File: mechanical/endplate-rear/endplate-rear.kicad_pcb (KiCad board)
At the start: 2 copper layers, 88 x 38 mm, 0 parts

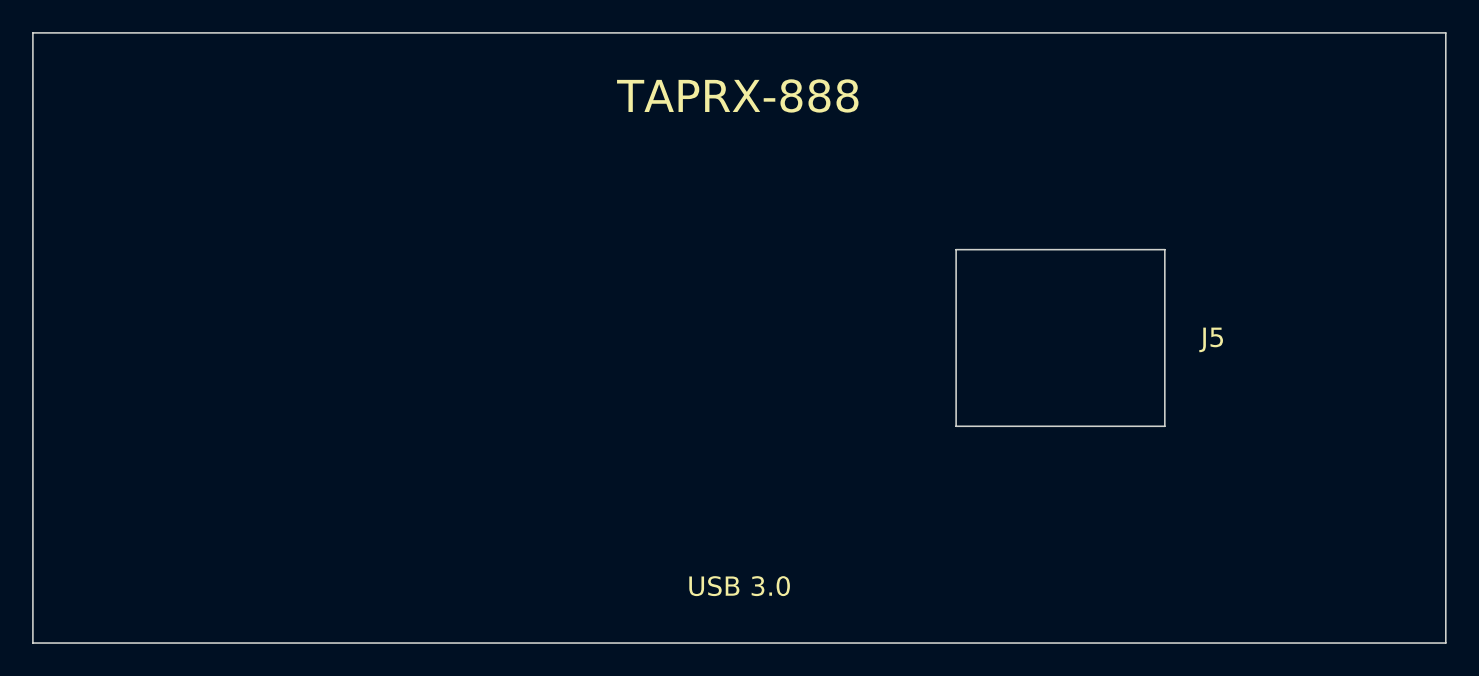
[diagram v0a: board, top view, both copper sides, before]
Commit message: mechanical: rebuild end plates from enclosure DXF geometry
Replace the nominal 88x38 starter outline with real geometry sectioned from the
enclosure extrusion end (FreeCAD DXF, centred on 0,0):

- outline 88x38 mm, corner radius 4.5 (rounded rect: 4 edges + 4 arcs)
- four M3 corner mounting holes, Ø3.4 at (±41, ±14.21) -> the plate screws on;
  it is not a slide-in panel (the 84.2 mm groove is the internal PCB slot)

Connector cutout X's are the main board's real connector positions mapped to
plate-centred coords (plate-X = 44 + (board-X - 138)), verified against the PCB:

- front SMA J1/J3/J2/J4 at -27/-9/+9/+26.8 mm from centre
- rear USB J5 at +19 mm from centre; J11 (JTAG) internal, no cutout

Connector Y remains a placeholder at plate centre pending the PCB rail height +
connector centre heights (3D models); cutout sizes (SMA Ø6.5, USB 13x11) and the
rear X-mirror stay flagged on Cmts.User. Open in KiCad 10 to confirm it parses.

Co-Authored-By: Claude Opus 4.8 <noreply@anthropic.com>
Claude-Session: https://claude.ai/code/session_019A4jkTeNPLki8CdfTWEUwM
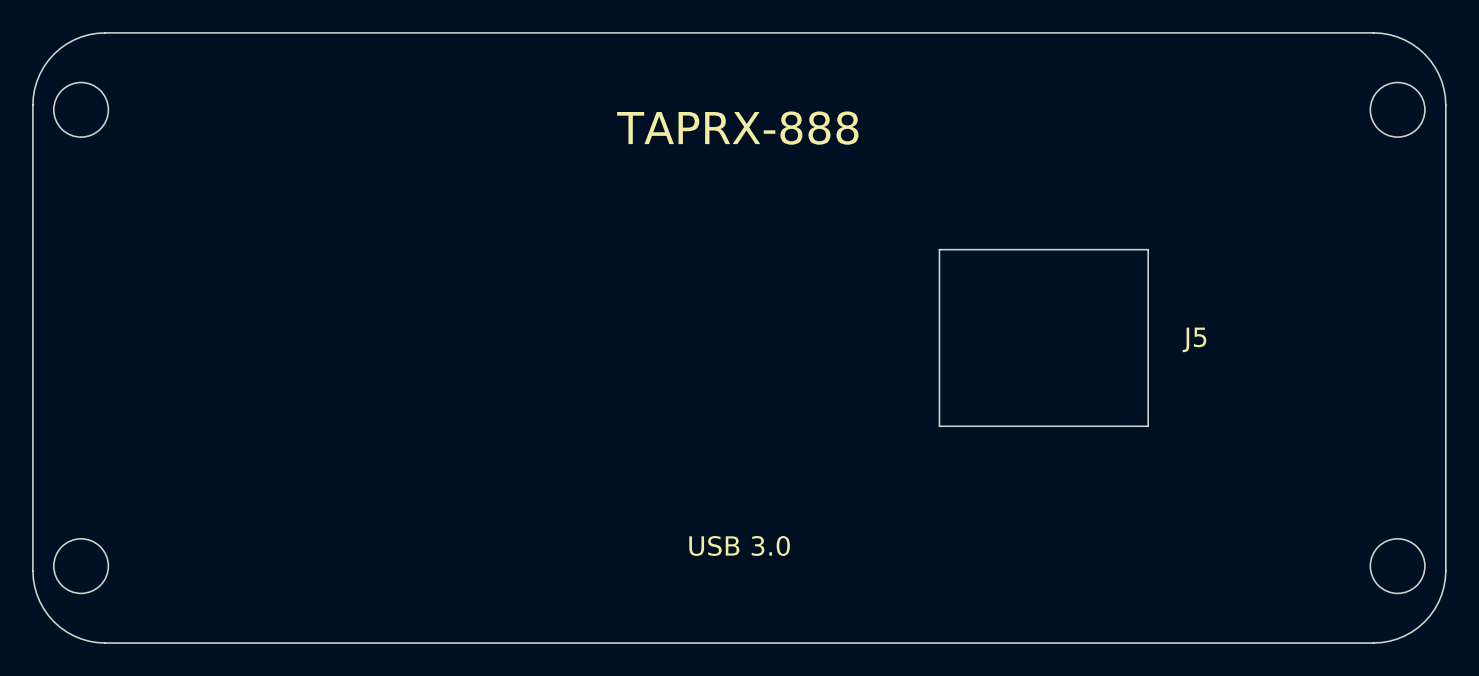
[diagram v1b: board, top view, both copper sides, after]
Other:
- outline, holes or cut-outs redrawn
- board text added: "REAR PLATE: confirm X-mirror vs assembly orientation. Outline+M3 corner holes from enclosure DXF (88x38 R4.5, holes Ø3.4 @ +/-41,+/-14.21). CONNECTOR Y IS PLACEHOLDER at plate centre -- set from PCB rail height + connector centre heights (3D models). SMA Ø6.5 / USB 13x11 verify vs parts. Open in KiCad 10 to confirm parse."
- board text removed: "REAR PLATE: confirm X-mirror vs assembly orientation. PLACEHOLDER GEOMETRY - verify vs enclosure STEP: plate 88x38 nominal (check groove fit); connector Y at plate centre (needs board height in rail + connector centre height); SMA D6.5 / USB 13x11 (verify vs parts)."
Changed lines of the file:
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@@
 		(company "TAPR")
 		(comment 1 "Non-functional enclosure end plate")
-		(comment 2 "Starter geometry -- verify against enclosure STEP")
+		(comment 2 "Outline+holes from enclosure DXF; connector Y placeholder")
 	)
 	(layers
@@
 	(net 0 "")
 	(gr_line
-		(start 0 0)
-		(end 88.0 0)
-		(stroke
-			(width 0.1)
-			(type default)
-		)
-		(layer "Edge.Cuts")
-	)
-	(gr_line
-		(start 88.0 0)
-		(end 88.0 38.0)
-		(stroke
-			(width 0.1)
-			(type default)
-		)
-		(layer "Edge.Cuts")
-	)
-	(gr_line
-		(start 88.0 38.0)
-		(end 0 38.0)
-		(stroke
-			(width 0.1)
-			(type default)
-		)
-		(layer "Edge.Cuts")
-	)
-	(gr_line
-		(start 0 38.0)
-		(end 0 0)
-		(stroke
-			(width 0.1)
-			(type default)
-		)
-		(layer "Edge.Cuts")
-	)
-	(gr_line
-		(start 57.5 13.5)
-		(end 70.5 13.5)
-		(stroke
-			(width 0.1)
-			(type default)
-		)
-		(layer "Edge.Cuts")
-	)
-	(gr_line
-		(start 70.5 13.5)
-		(end 70.5 24.5)
-		(stroke
-			(width 0.1)
-			(type default)
-		)
-		(layer "Edge.Cuts")
-	)
-	(gr_line
-		(start 70.5 24.5)
-		(end 57.5 24.5)
-		(stroke
-			(width 0.1)
-			(type default)
-		)
-		(layer "Edge.Cuts")
-	)
-	(gr_line
-		(start 57.5 24.5)
-		(end 57.5 13.5)
+		(start 4.5 0)
+		(end 83.5 0)
+		(stroke
+			(width 0.1)
+			(type default)
+		)
+		(layer "Edge.Cuts")
+	)
+	(gr_line
+		(start 88.0 4.5)
+		(end 88.0 33.5)
+		(stroke
+			(width 0.1)
+			(type default)
+		)
+		(layer "Edge.Cuts")
+	)
+	(gr_line
+		(start 83.5 38.0)
+		(end 4.5 38.0)
+		(stroke
+			(width 0.1)
+			(type default)
+		)
+		(layer "Edge.Cuts")
+	)
+	(gr_line
+		(start 0 33.5)
+		(end 0 4.5)
+		(stroke
+			(width 0.1)
+			(type default)
+		)
+		(layer "Edge.Cuts")
+	)
+	(gr_arc
+		(start 0 4.5)
+		(mid 1.318 1.318)
+		(end 4.5 0)
+		(stroke
+			(width 0.1)
+			(type default)
+		)
+		(layer "Edge.Cuts")
+	)
+	(gr_arc
+		(start 83.5 0)
+		(mid 86.682 1.318)
+		(end 88.0 4.5)
+		(stroke
+			(width 0.1)
+			(type default)
+		)
+		(layer "Edge.Cuts")
+	)
+	(gr_arc
+		(start 88.0 33.5)
+		(mid 86.682 36.682)
+		(end 83.5 38.0)
+		(stroke
+			(width 0.1)
+			(type default)
+		)
+		(layer "Edge.Cuts")
+	)
+	(gr_arc
+		(start 4.5 38.0)
+		(mid 1.318 36.682)
+		(end 0 33.5)
+		(stroke
+			(width 0.1)
+			(type default)
+		)
+		(layer "Edge.Cuts")
+	)
+	(gr_circle
+		(center 3.0 4.79)
+		(end 4.7 4.79)
+		(stroke
+			(width 0.1)
+			(type default)
+		)
+		(fill no)
+		(layer "Edge.Cuts")
+	)
+	(gr_circle
+		(center 85.0 4.79)
+		(end 86.7 4.79)
+		(stroke
+			(width 0.1)
+			(type default)
+		)
+		(fill no)
+		(layer "Edge.Cuts")
+	)
+	(gr_circle
+		(center 3.0 33.21)
+		(end 4.7 33.21)
+		(stroke
+			(width 0.1)
+			(type default)
+		)
+		(fill no)
+		(layer "Edge.Cuts")
+	)
+	(gr_circle
+		(center 85.0 33.21)
+		(end 86.7 33.21)
+		(stroke
+			(width 0.1)
+			(type default)
+		)
+		(fill no)
+		(layer "Edge.Cuts")
+	)
+	(gr_line
+		(start 56.462 13.5)
+		(end 69.462 13.5)
+		(stroke
+			(width 0.1)
+			(type default)
+		)
+		(layer "Edge.Cuts")
+	)
+	(gr_line
+		(start 69.462 13.5)
+		(end 69.462 24.5)
+		(stroke
+			(width 0.1)
+			(type default)
+		)
+		(layer "Edge.Cuts")
+	)
+	(gr_line
+		(start 69.462 24.5)
+		(end 56.462 24.5)
+		(stroke
+			(width 0.1)
+			(type default)
+		)
+		(layer "Edge.Cuts")
+	)
+	(gr_line
+		(start 56.462 24.5)
+		(end 56.462 13.5)
 		(stroke
 			(width 0.1)
@@
 	)
 	(gr_text "J5"
-		(at 73.5 19.0)
+		(at 72.462 19.0)
 		(layer "F.SilkS")
 		(effects
@@
 	)
 	(gr_text "TAPRX-888"
-		(at 44.0 4)
+		(at 44.0 6.0)
 		(layer "F.SilkS")
 		(effects
@@
 	)
 	(gr_text "USB 3.0"
-		(at 44.0 34.5)
+		(at 44.0 32.0)
 		(layer "F.SilkS")
 		(effects
@@
 		)
 	)
-	(gr_text "REAR PLATE: confirm X-mirror vs assembly orientation. PLACEHOLDER GEOMETRY - verify vs enclosure STEP: plate 88x38 nominal (check groove fit); connector Y at plate centre (needs board height in rail + connector centre height); SMA D6.5 / USB 13x11 (verify vs parts)."
+	(gr_text "REAR PLATE: confirm X-mirror vs assembly orientation. Outline+M3 corner holes from enclosure DXF (88x38 R4.5, holes Ø3.4 @ +/-41,+/-14.21). CONNECTOR Y IS PLACEHOLDER at plate centre -- set from PCB rail height + connector centre heights (3D models). SMA Ø6.5 / USB 13x11 verify vs parts. Open in KiCad 10 to confirm parse."
 		(at 44.0 42.0)
 		(layer "Cmts.User")

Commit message: mechanical: set end-plate connector Y from measured 7.9mm rail height
Drop the connector cutouts from their placeholder plate-centre position to their
real vertical location: the PCB rail sits 7.9mm above the enclosure floor
(measured), so with the floor at the plate's bottom edge the connector centres
land at plate Y = 30.12 (front SMA holes and rear USB opening alike). Add an
'ENCLOSURE FLOOR' silk marker on the bottom edge to pin orientation, and bump the
outline to the measured 38.02mm height. Connectors clear the bottom corner screws
(those sit at the far corners).

The SMA axis is ~the board plane; a USB connector body sits above the board
plane, so that opening's centre rises once the connector height is known -- left
flagged with the cutout-size placeholders (SMA Ø6.5 / USB 13x11) and the rear
X-mirror. README updated: connector Y is now set, not a placeholder.

Co-Authored-By: Claude Opus 4.8 <noreply@anthropic.com>
Claude-Session: https://claude.ai/code/session_019A4jkTeNPLki8CdfTWEUwM
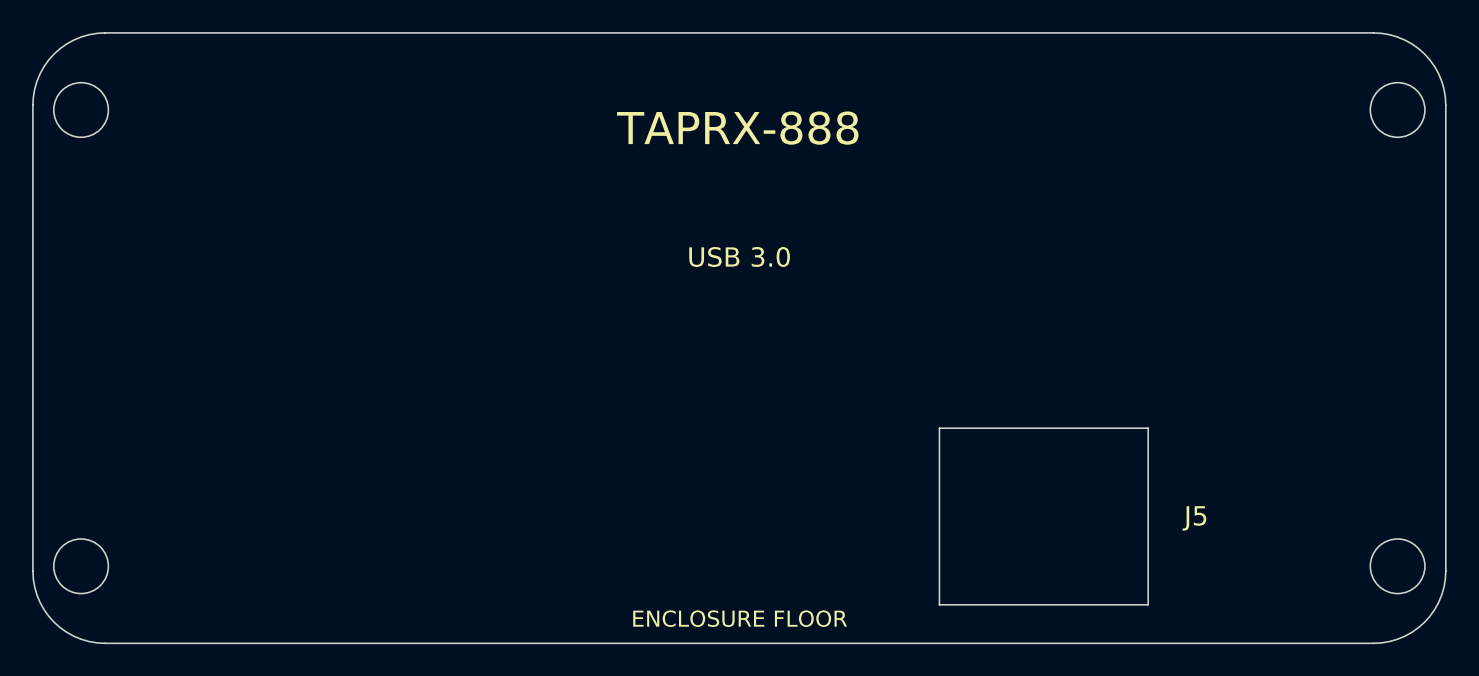
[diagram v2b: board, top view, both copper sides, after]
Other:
- outline, holes or cut-outs redrawn
- board text added: "ENCLOSURE FLOOR"
- board text added: "REAR PLATE: confirm X-mirror vs assembly orientation. Outline+M3 corner holes from enclosure DXF (88x38 R4.5, holes Ø3.4 @ +/-41,+/-14.21). Connector Y set from measured 7.9mm PCB rail height above enclosure floor (bottom edge) -> plate Y 30.12. SMA axis ~board plane; USB opening sits ABOVE board plane by connector body height (part-specific, TBD). SMA Ø6.5 / USB 13x11 verify vs parts. Open in Ki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"
- board text removed: "REAR PLATE: confirm X-mirror vs assembly orientation. Outline+M3 corner holes from enclosure DXF (88x38 R4.5, holes Ø3.4 @ +/-41,+/-14.21). CONNECTOR Y IS PLACEHOLDER at plate centre -- set from PCB rail height + connector centre heights (3D models). SMA Ø6.5 / USB 13x11 verify vs parts. Open in KiCad 10 to confirm parse."
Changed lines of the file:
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@@
 	(gr_line
 		(start 88.0 4.5)
-		(end 88.0 33.5)
+		(end 88.0 33.52)
 		(stroke
 			(width 0.1)
@@
 	)
 	(gr_line
-		(start 83.5 38.0)
-		(end 4.5 38.0)
+		(start 83.5 38.02)
+		(end 4.5 38.02)
 		(stroke
 			(width 0.1)
@@
 	)
 	(gr_line
-		(start 0 33.5)
+		(start 0 33.52)
 		(end 0 4.5)
 		(stroke
@@
 	)
 	(gr_arc
-		(start 88.0 33.5)
-		(mid 86.682 36.682)
-		(end 83.5 38.0)
+		(start 88.0 33.52)
+		(mid 86.682 36.702)
+		(end 83.5 38.02)
 		(stroke
 			(width 0.1)
@@
 	)
 	(gr_arc
-		(start 4.5 38.0)
-		(mid 1.318 36.682)
-		(end 0 33.5)
+		(start 4.5 38.02)
+		(mid 1.318 36.702)
+		(end 0 33.52)
 		(stroke
 			(width 0.1)
@@
 	)
 	(gr_circle
-		(center 3.0 4.79)
-		(end 4.7 4.79)
+		(center 3.0 4.8)
+		(end 4.7 4.8)
 		(stroke
 			(width 0.1)
@@
 	)
 	(gr_circle
-		(center 85.0 4.79)
-		(end 86.7 4.79)
+		(center 85.0 4.8)
+		(end 86.7 4.8)
 		(stroke
 			(width 0.1)
@@
 	)
 	(gr_circle
-		(center 3.0 33.21)
-		(end 4.7 33.21)
+		(center 3.0 33.22)
+		(end 4.7 33.22)
 		(stroke
 			(width 0.1)
@@
 	)
 	(gr_circle
-		(center 85.0 33.21)
-		(end 86.7 33.21)
+		(center 85.0 33.22)
+		(end 86.7 33.22)
 		(stroke
 			(width 0.1)
@@
 	)
 	(gr_line
-		(start 56.462 13.5)
-		(end 69.462 13.5)
+		(start 56.462 24.62)
+		(end 69.462 24.62)
 		(stroke
 			(width 0.1)
@@
 	)
 	(gr_line
-		(start 69.462 13.5)
-		(end 69.462 24.5)
+		(start 69.462 24.62)
+		(end 69.462 35.62)
 		(stroke
 			(width 0.1)
@@
 	)
 	(gr_line
-		(start 69.462 24.5)
-		(end 56.462 24.5)
+		(start 69.462 35.62)
+		(end 56.462 35.62)
 		(stroke
 			(width 0.1)
@@
 	)
 	(gr_line
-		(start 56.462 24.5)
-		(end 56.462 13.5)
+		(start 56.462 35.62)
+		(end 56.462 24.62)
 		(stroke
 			(width 0.1)
@@
 	)
 	(gr_text "J5"
-		(at 72.462 19.0)
+		(at 72.462 30.12)
 		(layer "F.SilkS")
 		(effects
@@
 	)
 	(gr_text "TAPRX-888"
-		(at 44.0 6.0)
+		(at 44.0 6)
 		(layer "F.SilkS")
 		(effects
@@
 	)
 	(gr_text "USB 3.0"
-		(at 44.0 32.0)
+		(at 44.0 14)
 		(layer "F.SilkS")
 		(effects
@@
 		)
 	)
-	(gr_text "REAR PLATE: confirm X-mirror vs assembly orientation. Outline+M3 corner holes from enclosure DXF (88x38 R4.5, holes Ø3.4 @ +/-41,+/-14.21). CONNECTOR Y IS PLACEHOLDER at plate centre -- set from PCB rail height + connector centre heights (3D models). SMA Ø6.5 / USB 13x11 verify vs parts. Open in KiCad 10 to confirm parse."
-		(at 44.0 42.0)
+	(gr_text "ENCLOSURE FLOOR"
+		(at 44.0 36.52)
+		(layer "F.SilkS")
+		(effects
+			(font
+				(size 1.0 1.0)
+				(thickness 0.15)
+			)
+		)
+	)
+	(gr_text "REAR PLATE: confirm X-mirror vs assembly orientation. Outline+M3 corner holes from enclosure DXF (88x38 R4.5, holes Ø3.4 @ +/-41,+/-14.21). Connector Y set from measured 7.9mm PCB rail height above enclosure floor (bottom edge) -> plate Y 30.12. SMA axis ~board plane; USB opening sits ABOVE board plane by connector body height (part-specific, TBD). SMA Ø6.5 / USB 13x11 verify vs parts. Open in KiCad 10 to confirm parse."
+		(at 44.0 42.02)
 		(layer "Cmts.User")
 		(effects
